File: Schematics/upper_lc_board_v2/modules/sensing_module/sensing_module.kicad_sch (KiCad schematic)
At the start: 19 parts, among them J5 HALL-1, U7 ADC_ADS131M04IPWR

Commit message: review work
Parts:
- removed D16, D17, D18: LED, LED_SMD:LED_0603_1608Metric, symbol Device:LED
- removed R26, R40, R41: 150, Resistor_SMD:R_0603_1608Metric, symbol Device:R
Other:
- note removed: "Sensing Indication"

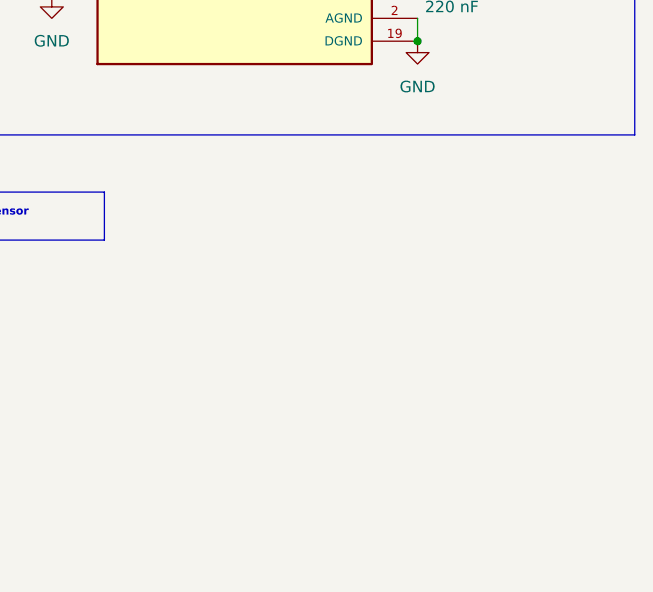
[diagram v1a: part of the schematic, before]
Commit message: add additional LEDs
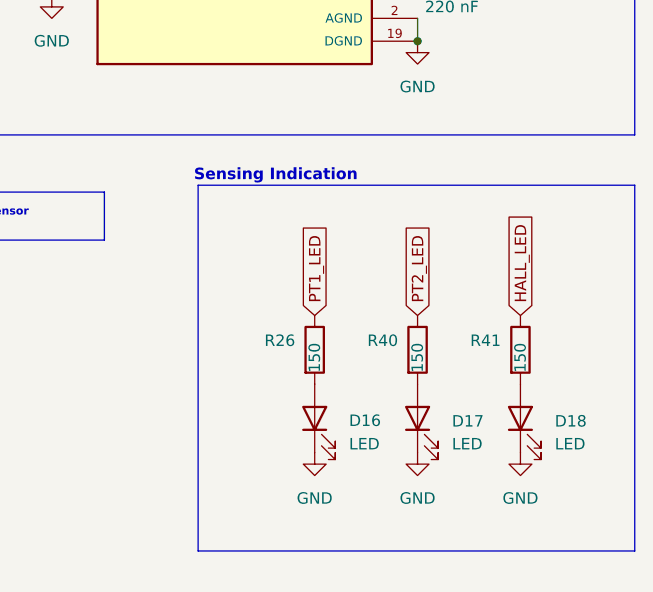
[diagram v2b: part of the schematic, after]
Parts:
- added D16, D17, D18: LED, LED_SMD:LED_0603_1608Metric, symbol Device:LED
- added R26, R40, R41: 150, Resistor_SMD:R_0603_1608Metric, symbol Device:R
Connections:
- net GND: now also D16.1 (K), D17.1 (K), D18.1 (K)
- new net: D17.2 (A), R40.2
- new net: D16.2 (A), R26.2
- new net: D18.2 (A), R41.2
- new net HALL_LED: R41.1
- new net PT1_LED: R26.1
- new net PT2_LED: R40.1
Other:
- note added: "Sensing Indication"
